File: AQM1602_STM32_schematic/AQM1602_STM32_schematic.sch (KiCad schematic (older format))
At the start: 7 parts, among them J1 AQM1602, P1 NUCLEO_F411RE

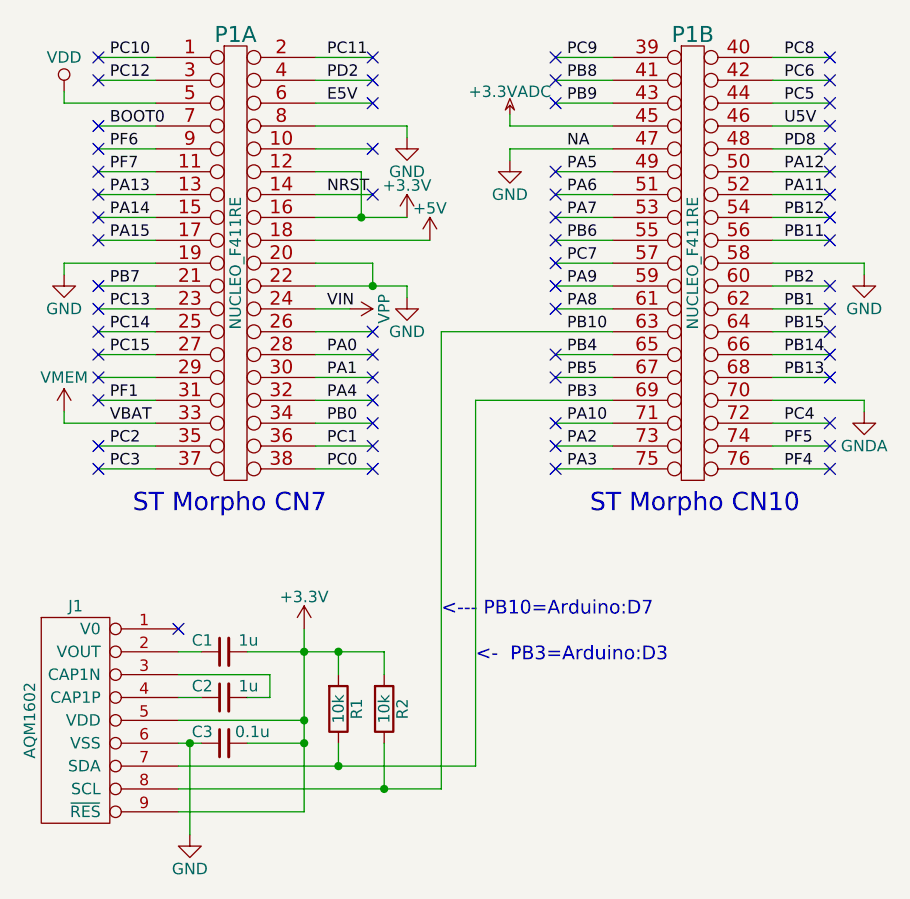
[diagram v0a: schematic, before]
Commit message: fix pin name
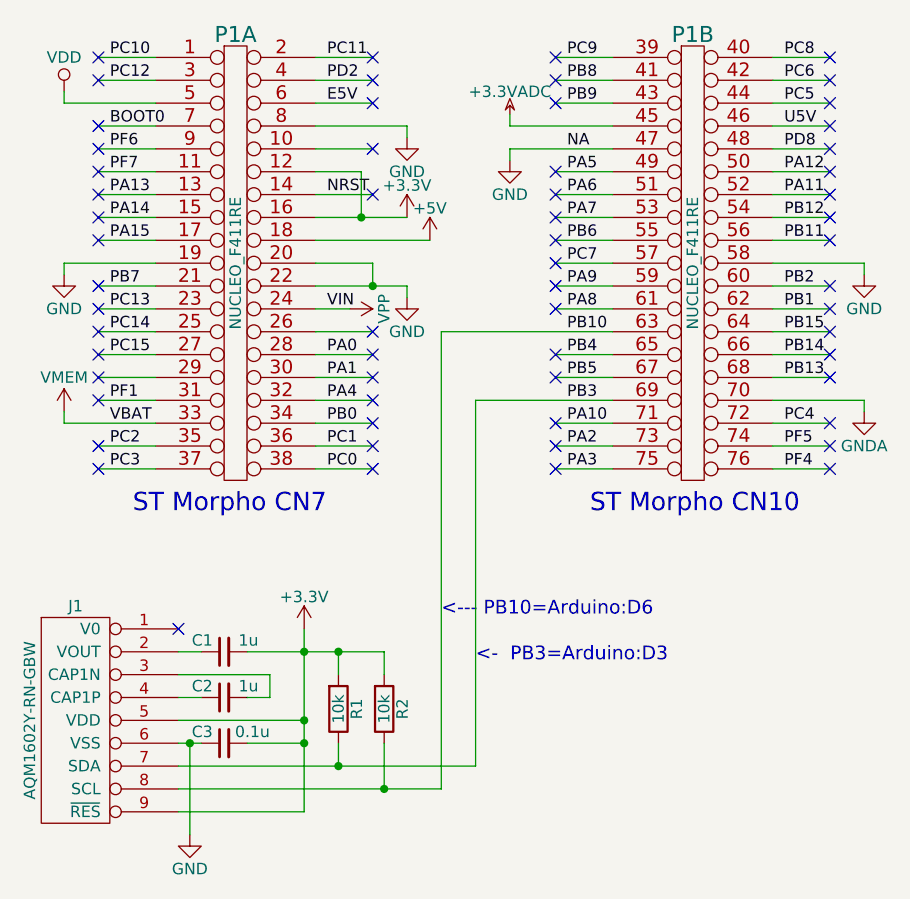
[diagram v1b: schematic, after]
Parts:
- J1: value AQM1602 -> AQM1602Y-RN-GBW
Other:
- note added: "<--- PB10=Arduino:D6"
- note removed: "<--- PB10=Arduino:D7"
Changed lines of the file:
@@
 P 2700 6000
 F 0 "J1" H 2700 6500 50  0000 C CNN
-F 1 "AQM1602" V 2500 6000 50  0000 C CNN
+F 1 "AQM1602Y-RN-GBW" V 2500 6000 50  0000 C CNN
 F 2 "" H 2700 6000 50  0000 C CNN
 F 3 "" H 2700 6000 50  0000 C CNN
@@
 Connection ~ 3850 6200
 Text Notes 4300 5550 0    60   ~ 0
-<--- PB10=Arduino:D7
+<--- PB10=Arduino:D6
 Text Notes 4450 5750 0    60   ~ 0
 <-  PB3=Arduino:D3
